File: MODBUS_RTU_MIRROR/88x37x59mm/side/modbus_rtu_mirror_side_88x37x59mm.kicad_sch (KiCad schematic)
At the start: 38 parts, among them J1 Conn_01x04_Male, J2 Conn_01x04_Male, J3 Conn_01x06_Male, SW1 SW_Push, U1 ESP32-WROOM-32, U2 TXS0108EPW, U3 AMS1117-3.3, U4 DS3231MZ, U5 FM24C64C

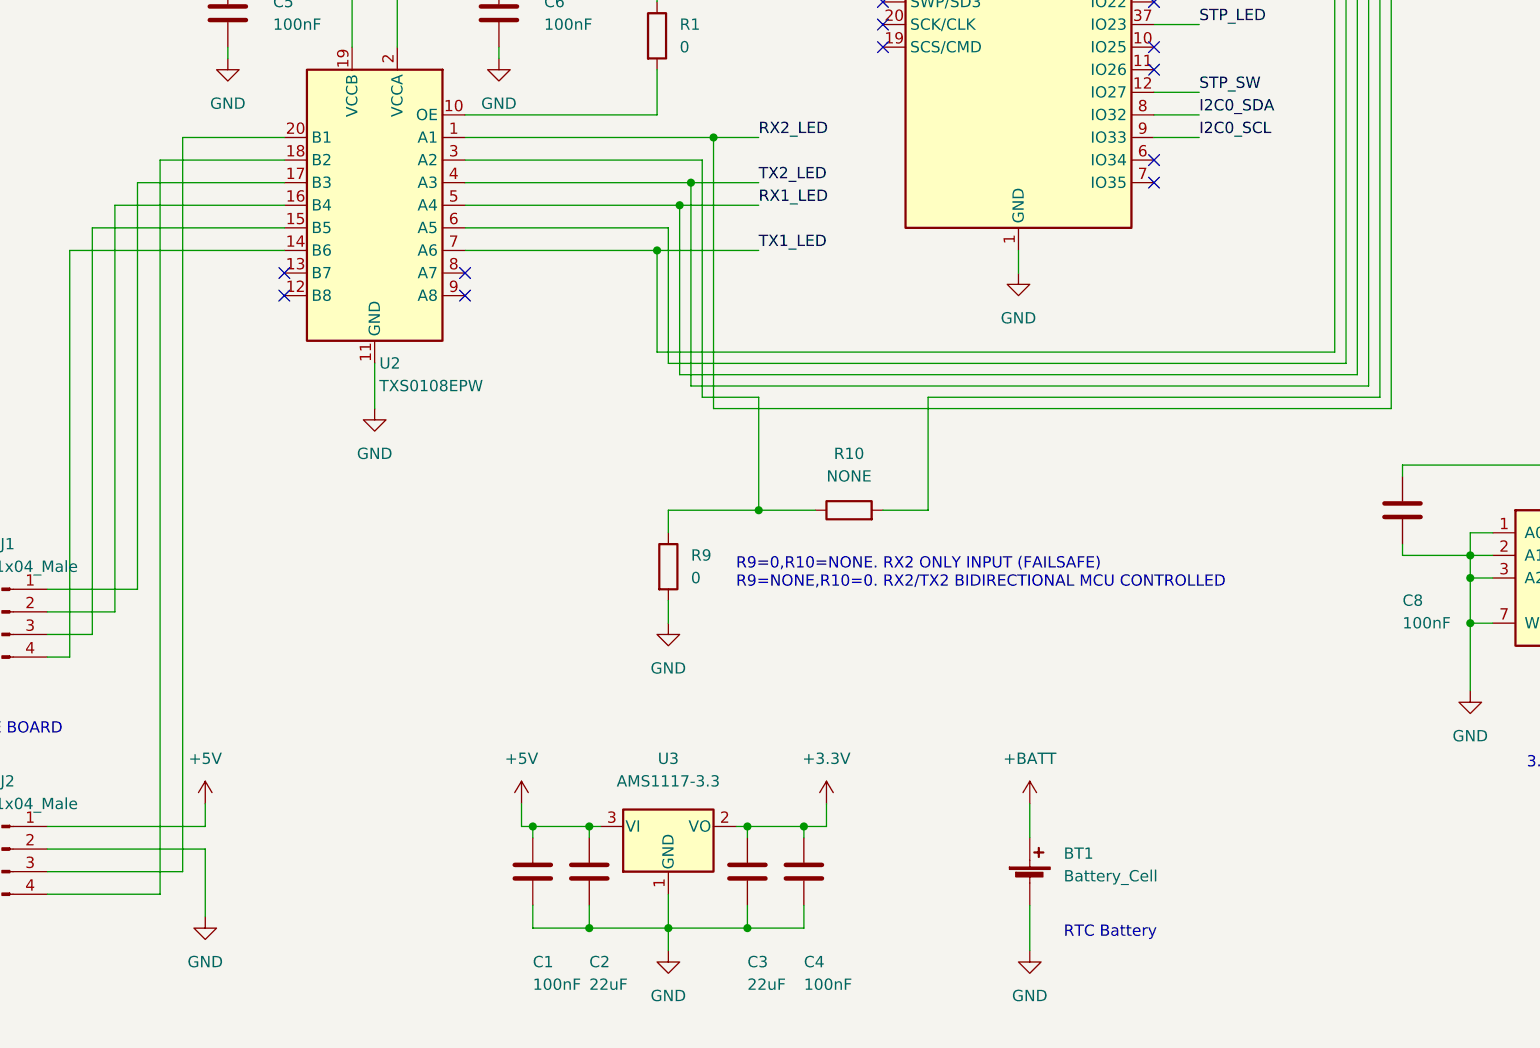
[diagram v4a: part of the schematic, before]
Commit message: all traces routed
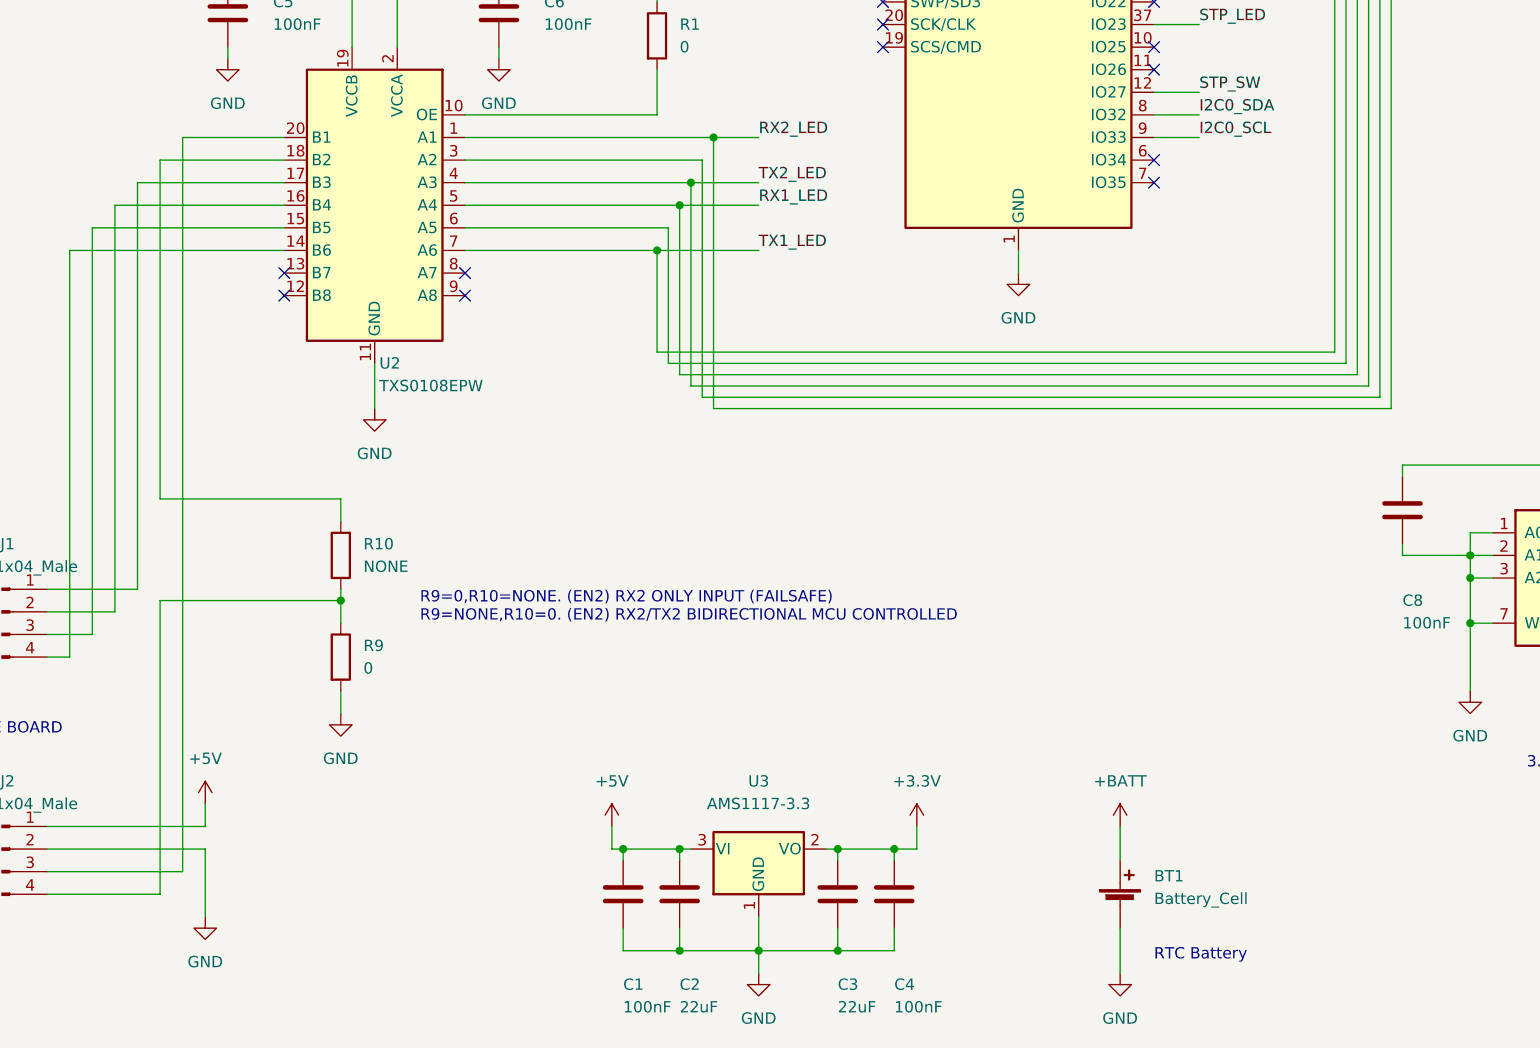
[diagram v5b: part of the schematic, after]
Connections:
- net at U2.18 (B2): now also R10.2; no longer J2.4 (Pin_4)
- net at R10.1, R9.1: now also J2.4 (Pin_4); no longer U2.3 (A2)
- net at U1.27 (IO16): now also U2.3 (A2); no longer R10.2
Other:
- note added: "R9=0,R10=NONE. (EN2) RX2 ONLY INPUT (FAILSAFE) R9=NONE,R10=0. (EN2) RX2/TX2 BIDIRECTIONAL MCU CONTROLLED"
- note removed: "R9=0,R10=NONE. RX2 ONLY INPUT (FAILSAFE) R9=NONE,R10=0. RX2/TX2 BIDIRECTIONAL MCU CONTROLLED"
- moved on the sheet: BT1, C1, C2, C3, C4, R10, R9, U3
